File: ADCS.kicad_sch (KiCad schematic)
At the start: 16 parts

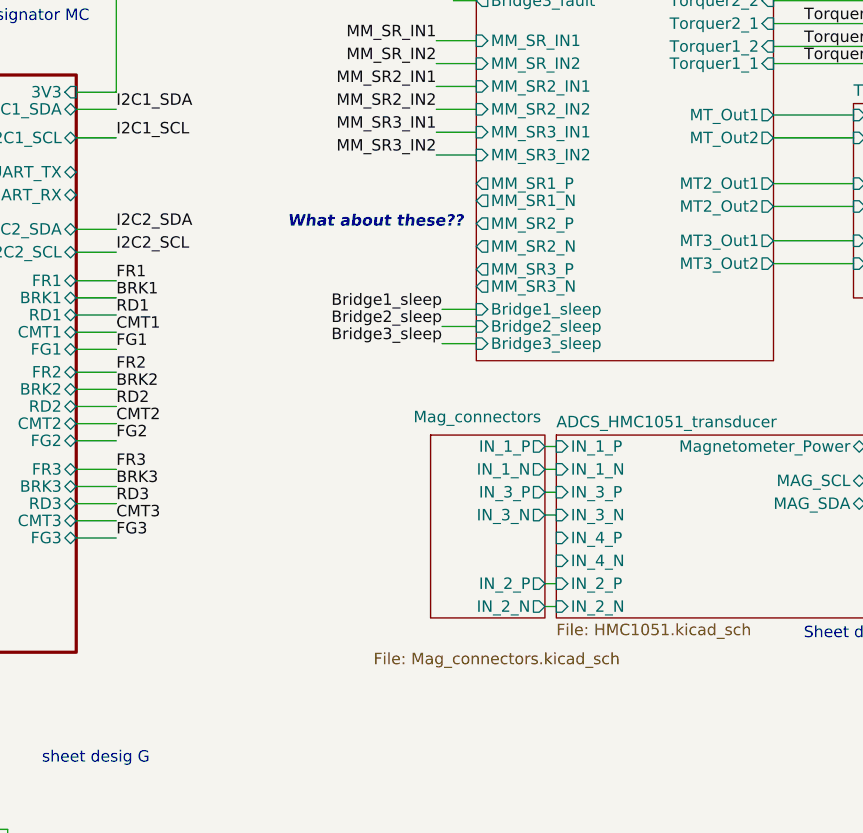
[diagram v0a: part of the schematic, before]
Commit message: Updated 8 pin connector for magentometer
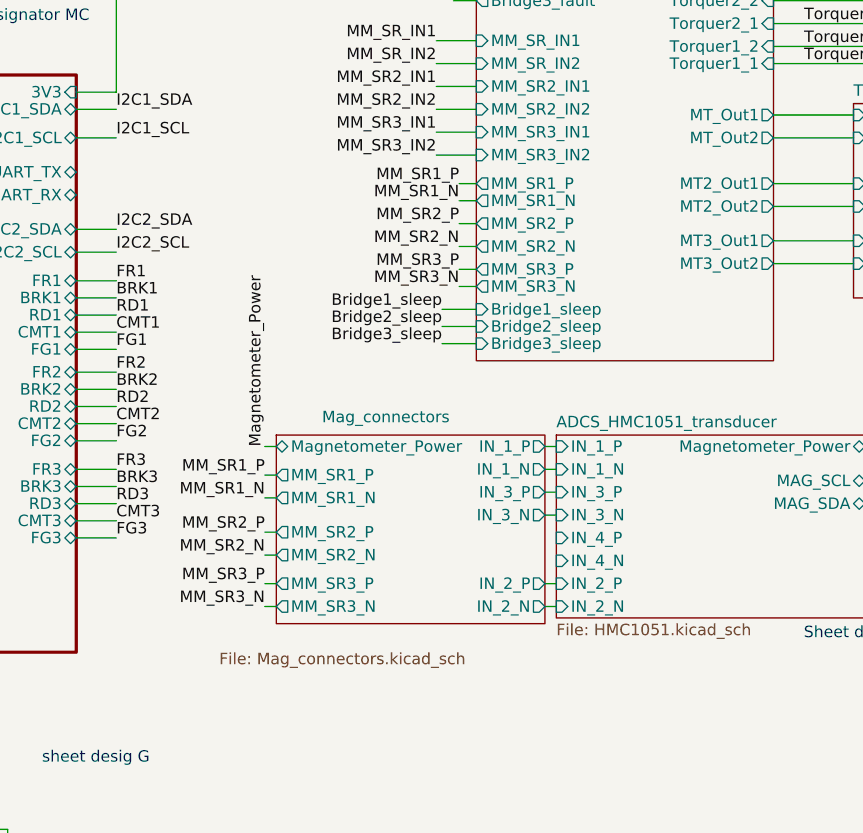
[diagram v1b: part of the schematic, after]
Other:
- sheet Mag_connectors ports: added MM_SR1_N, MM_SR1_P, MM_SR2_N, MM_SR2_P, MM_SR3_N, MM_SR3_P, Magnetometer_Power; removed none
- note removed: "What about these??"
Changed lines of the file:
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@@
     (stroke (width 0) (type default) (color 0 0 0 0))
   )
+  (wire (pts (xy 194.31 95.25) (xy 195.58 95.25))
+    (stroke (width 0) (type default) (color 0 0 0 0))
+  )
   (wire (pts (xy 215.265 38.1) (xy 217.805 38.1))
     (stroke (width 0) (type default) (color 0 0 0 0))
@@
     (stroke (width 0) (type default) (color 0 0 0 0))
   )
+  (wire (pts (xy 194.31 92.71) (xy 195.58 92.71))
+    (stroke (width 0) (type default) (color 0 0 0 0))
+  )
   (wire (pts (xy 157.48 33.655) (xy 161.29 33.655))
     (stroke (width 0) (type default) (color 0 0 0 0))
@@
     (stroke (width 0) (type default) (color 0 0 0 0))
   )
+  (wire (pts (xy 215.9 60.325) (xy 217.805 60.325))
+    (stroke (width 0) (type default) (color 0 0 0 0))
+  )
   (wire (pts (xy 161.925 135.89) (xy 161.925 139.7))
     (stroke (width 0) (type default) (color 0 0 0 0))
@@
     (stroke (width 0) (type default) (color 0 0 0 0))
   )
+  (wire (pts (xy 215.9 67.31) (xy 217.805 67.31))
+    (stroke (width 0) (type default) (color 0 0 0 0))
+  )
+  (wire (pts (xy 215.9 62.23) (xy 217.805 62.23))
+    (stroke (width 0) (type default) (color 0 0 0 0))
+  )
+  (wire (pts (xy 215.9 71.755) (xy 217.805 71.755))
+    (stroke (width 0) (type default) (color 0 0 0 0))
+  )
   (wire (pts (xy 19.685 80.01) (xy 23.495 80.01))
     (stroke (width 0) (type default) (color 0 0 0 0))
@@
     (stroke (width 0) (type default) (color 0 0 0 0))
   )
+  (wire (pts (xy 194.31 89.535) (xy 195.58 89.535))
+    (stroke (width 0) (type default) (color 0 0 0 0))
+  )
   (wire (pts (xy 127 105.41) (xy 130.81 105.41))
     (stroke (width 0) (type default) (color 0 0 0 0))
@@
     (stroke (width 0) (type default) (color 0 0 0 0))
   )
+  (wire (pts (xy 215.9 69.85) (xy 217.805 69.85))
+    (stroke (width 0) (type default) (color 0 0 0 0))
+  )
   (wire (pts (xy 22.225 100.33) (xy 23.495 100.33))
     (stroke (width 0) (type default) (color 0 0 0 0))
@@
     (stroke (width 0) (type default) (color 0 0 0 0))
   )
+  (wire (pts (xy 194.31 99.06) (xy 195.58 99.06))
+    (stroke (width 0) (type default) (color 0 0 0 0))
+  )
   (wire (pts (xy 48.895 102.87) (xy 48.895 92.71))
     (stroke (width 0) (type default) (color 0 0 0 0))
@@
     (stroke (width 0) (type default) (color 0 0 0 0))
   )
+  (wire (pts (xy 194.31 104.775) (xy 195.58 104.775))
+    (stroke (width 0) (type default) (color 0 0 0 0))
+  )
   (wire (pts (xy 121.92 130.81) (xy 126.365 130.81))
     (stroke (width 0) (type default) (color 0 0 0 0))
@@
     (stroke (width 0) (type default) (color 0 0 0 0))
   )
+  (wire (pts (xy 194.31 107.315) (xy 195.58 107.315))
+    (stroke (width 0) (type default) (color 0 0 0 0))
+  )
   (wire (pts (xy 215.265 36.195) (xy 217.805 36.195))
     (stroke (width 0) (type default) (color 0 0 0 0))
@@
     (stroke (width 0) (type default) (color 0 0 0 0))
   )
+  (wire (pts (xy 194.31 101.6) (xy 195.58 101.6))
+    (stroke (width 0) (type default) (color 0 0 0 0))
+  )
   (wire (pts (xy 173.355 71.12) (xy 177.8 71.12))
     (stroke (width 0) (type default) (color 0 0 0 0))
@@
     (stroke (width 0) (type default) (color 0 0 0 0))
   )
+  (wire (pts (xy 215.9 64.77) (xy 217.805 64.77))
+    (stroke (width 0) (type default) (color 0 0 0 0))
+  )
   (wire (pts (xy 60.325 72.39) (xy 62.865 72.39))
     (stroke (width 0) (type default) (color 0 0 0 0))
@@
     (effects (font (size 1.27 1.27)) (justify left bottom))
   )
-  (text "What about these??" (at 196.85 65.405 0)
-    (effects (font (size 1.27 1.27) (thickness 0.254) bold italic) (justify left bottom))
-  )
   (text "Sheet Designator R\n" (at 63.5 45.72 0)
     (effects (font (size 1.27 1.27)) (justify left bottom))
@@
     (effects (font (size 1.27 1.27)) (justify right bottom))
   )
+  (label "MM_SR1_N" (at 215.9 62.23 180)
+    (effects (font (size 1.27 1.27)) (justify right bottom))
+  )
   (label "I2C2_SDA" (at 102.235 21.59 180)
     (effects (font (size 1.27 1.27)) (justify right bottom))
@@
     (effects (font (size 1.27 1.27)) (justify right bottom))
   )
+  (label "MM_SR1_P" (at 215.9 60.325 180)
+    (effects (font (size 1.27 1.27)) (justify right bottom))
+  )
+  (label "MM_SR3_N" (at 194.31 107.315 180)
+    (effects (font (size 1.27 1.27)) (justify right bottom))
+  )
   (label "I2C1_SDA" (at 179.07 146.05 0)
     (effects (font (size 1.27 1.27)) (justify left bottom))
@@
     (effects (font (size 1.27 1.27)) (justify right bottom))
   )
+  (label "MM_SR2_P" (at 215.9 64.77 180)
+    (effects (font (size 1.27 1.27)) (justify right bottom))
+  )
   (label "MM_SR2_IN1" (at 128.27 84.455 180)
     (effects (font (size 1.27 1.27)) (justify right bottom))
@@
     (effects (font (size 1.27 1.27)) (justify right bottom))
   )
+  (label "MM_SR2_N" (at 215.9 67.31 180)
+    (effects (font (size 1.27 1.27)) (justify right bottom))
+  )
   (label "RD1" (at 177.8 74.93 0)
     (effects (font (size 1.27 1.27)) (justify left bottom))
@@
     (effects (font (size 1.27 1.27)) (justify left bottom))
   )
+  (label "MM_SR1_N" (at 194.31 95.25 180)
+    (effects (font (size 1.27 1.27)) (justify right bottom))
+  )
   (label "CMT1" (at 19.685 49.53 180)
     (effects (font (size 1.27 1.27)) (justify right bottom))
@@
     (effects (font (size 1.27 1.27)) (justify right bottom))
   )
+  (label "MM_SR3_N" (at 215.9 71.755 180)
+    (effects (font (size 1.27 1.27)) (justify right bottom))
+  )
   (label "V_bridge" (at 161.29 31.115 0)
     (effects (font (size 1.27 1.27)) (justify left bottom))
@@
     (effects (font (size 1.27 1.27)) (justify right bottom))
   )
+  (label "MM_SR1_P" (at 194.31 92.71 180)
+    (effects (font (size 1.27 1.27)) (justify right bottom))
+  )
   (label "MM_SR_IN1" (at 213.36 44.45 180)
     (effects (font (size 1.27 1.27)) (justify right bottom))
@@
     (effects (font (size 1.27 1.27)) (justify right bottom))
   )
+  (label "MM_SR3_P" (at 194.31 104.775 180)
+    (effects (font (size 1.27 1.27)) (justify right bottom))
+  )
   (label "MM_SR3_IN1" (at 213.36 54.61 180)
     (effects (font (size 1.27 1.27)) (justify right bottom))
   )
+  (label "MM_SR2_P" (at 194.31 99.06 180)
+    (effects (font (size 1.27 1.27)) (justify right bottom))
+  )
   (label "Bridge1_fault" (at 127 96.52 180)
     (effects (font (size 1.27 1.27)) (justify right bottom))
@@
     (effects (font (size 1.27 1.27)) (justify right bottom))
   )
+  (label "MM_SR2_N" (at 194.31 101.6 180)
+    (effects (font (size 1.27 1.27)) (justify right bottom))
+  )
   (label "MCU_POW" (at 22.225 71.12 180)
     (effects (font (size 1.27 1.27)) (justify right bottom))
@@
     (effects (font (size 1.143 1.143)) (justify right bottom))
   )
+  (label "MM_SR3_P" (at 215.9 69.85 180)
+    (effects (font (size 1.27 1.27)) (justify right bottom))
+  )
   (label "Bridge3_sleep" (at 213.995 78.105 180)
     (effects (font (size 1.27 1.27)) (justify right bottom))
@@
     (effects (font (size 1.27 1.27)) (justify left bottom))
   )
+  (label "Magnetometer_Power" (at 194.31 89.535 90)
+    (effects (font (size 1.27 1.27)) (justify left bottom))
+  )
   (label "I2C1_SCL" (at 177.8 142.875 0)
     (effects (font (size 1.27 1.27)) (justify left bottom))
@@
     )
   )
-  (sheet (at 212.725 88.265) (size 12.7 20.32)
+  (sheet (at 195.58 88.265) (size 29.845 20.955)
     (stroke (width 0.1524) (type solid) (color 0 0 0 0))
     (fill (color 173 230 255 1.0000))
-    (property "Sheet name" "Mag_connectors" (id 0) (at 210.82 86.995 0)
+    (property "Sheet name" "Mag_connectors" (id 0) (at 200.66 86.995 0)
       (effects (font (size 1.27 1.27)) (justify left bottom))
     )
-    (property "Sheet file" "Mag_connectors.kicad_sch" (id 1) (at 206.375 112.395 0)
+    (property "Sheet file" "Mag_connectors.kicad_sch" (id 1) (at 189.23 112.395 0)
       (effects (font (size 1.27 1.27)) (justify left top))
     )
@@
       (effects (font (size 1.27 1.27)) (justify right))
     )
+    (pin "Magnetometer_Power" bidirectional (at 195.58 89.535 180)
+      (effects (font (size 1.27 1.27)) (justify left))
+    )
+    (pin "MM_SR1_P" output (at 195.58 92.71 180)
+      (effects (font (size 1.27 1.27)) (justify left))
+    )
+    (pin "MM_SR3_P" output (at 195.58 104.775 180)
+      (effects (font (size 1.27 1.27)) (justify left))
+    )
+    (pin "MM_SR2_N" output (at 195.58 101.6 180)
+      (effects (font (size 1.27 1.27)) (justify left))
+    )
+    (pin "MM_SR1_N" output (at 195.58 95.25 180)
+      (effects (font (size 1.27 1.27)) (justify left))
+    )
+    (pin "MM_SR2_P" output (at 195.58 99.06 180)
+      (effects (font (size 1.27 1.27)) (justify left))
+    )
+    (pin "MM_SR3_N" output (at 195.58 107.315 180)
+      (effects (font (size 1.27 1.27)) (justify left))
+    )
   )
   (sheet (at 226.695 88.265) (size 34.29 20.32) (fields_autoplaced)
@@
       (reference "#PWR0264") (unit 1) (value "GND") (footprint "")
     )
+    (path "/90eea1cc-3897-47cb-b6ba-95228c17b7e0/9b0b7e65-9fe2-4923-805e-2058d79ef8cd"
+      (reference "#PWR?") (unit 1) (value "GND") (footprint "")
+    )
+    (path "/90eea1cc-3897-47cb-b6ba-95228c17b7e0/fee31364-d497-434e-aba3-d9001da3381e"
+      (reference "#PWR?") (unit 1) (value "GND") (footprint "")
+    )
     (path "/85fce53c-db5d-41a5-af86-f02ad1af70e7/c2b51706-9b59-4979-b562-badd0d98848a"
       (reference "CA3") (unit 1) (value "2.2u") (footprint "")
@@
       (reference "JSC6") (unit 1) (value "2367196-8") (footprint "")
     )
+    (path "/90eea1cc-3897-47cb-b6ba-95228c17b7e0/a754a1e4-2f8d-40cf-a07f-bdf1f085778f"
+      (reference "JSC?") (unit 1) (value "2367196-8") (footprint "")
+    )
     (path "/4d1fba12-6ef0-42d4-9064-f9f362dde9b9/8656cb07-b7b7-4825-942a-87872d0ebb27"

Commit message: Updated the changes
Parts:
- gave numbers to parts that had none: 2
- renumbered R7 to R10, R8 to R11, R9 to R12, R10 to R13, R11 to R14, R14 to R2, R2 to R3, R3 to R4, R4 to R5, R5 to R6, R12 to R7, R13 to R8, R6 to R9
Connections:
- no-connect marks 0 -> 4

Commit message: magnetometer connector corrected
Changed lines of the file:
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@@
     (effects (font (size 1.27 1.27)) (justify left bottom))
   )
-  (text "sheet desig G\n\n" (at 169.545 127 0)
+  (text "sheet desig G\n\n" (at 200.66 119.38 0)
     (effects (font (size 1.27 1.27)) (justify left bottom))
   )
@@
       (reference "#PWR0149") (unit 1) (value "GND") (footprint "")
     )
-    (path "/90eea1cc-3897-47cb-b6ba-95228c17b7e0/af365d8d-45a0-4279-b9aa-e85ef081cff1"
-      (reference "#PWR0150") (unit 1) (value "GND") (footprint "")
-    )
-    (path "/90eea1cc-3897-47cb-b6ba-95228c17b7e0/9b0b7e65-9fe2-4923-805e-2058d79ef8cd"
-      (reference "#PWR0151") (unit 1) (value "GND") (footprint "")
-    )
-    (path "/90eea1cc-3897-47cb-b6ba-95228c17b7e0/fee31364-d497-434e-aba3-d9001da3381e"
-      (reference "#PWR0152") (unit 1) (value "GND") (footprint "")
-    )
-    (path "/90eea1cc-3897-47cb-b6ba-95228c17b7e0/d212d134-095c-4203-b1ec-5eee87c1621f"
-      (reference "#PWR0153") (unit 1) (value "GND") (footprint "")
-    )
-    (path "/90eea1cc-3897-47cb-b6ba-95228c17b7e0/b3290ea7-02f6-47a6-9a50-5235251e13f0"
-      (reference "#PWR0154") (unit 1) (value "GND") (footprint "")
-    )
     (path "/7a353e73-f362-4813-b2c3-9e73ce7ee8de/2e2e80b8-f5cb-4c8f-ae78-85b5504fc930"
       (reference "#PWR0155") (unit 1) (value "GND") (footprint "")
@@
       (reference "#PWR0166") (unit 1) (value "GND") (footprint "")
     )
+    (path "/90eea1cc-3897-47cb-b6ba-95228c17b7e0/08c4494f-9f1c-4926-98e0-493f36ae8c45"
+      (reference "#PWR?") (unit 1) (value "GND") (footprint "")
+    )
+    (path "/90eea1cc-3897-47cb-b6ba-95228c17b7e0/1252f635-9880-4113-b5ba-9f84c80cbab9"
+      (reference "#PWR?") (unit 1) (value "GND") (footprint "")
+    )
+    (path "/90eea1cc-3897-47cb-b6ba-95228c17b7e0/35c6e339-688e-4d33-b782-0f842ecaf145"
+      (reference "#PWR?") (unit 1) (value "GND") (footprint "")
+    )
+    (path "/90eea1cc-3897-47cb-b6ba-95228c17b7e0/88ef94b4-1b3f-401a-83e5-5c6f167ecc62"
+      (reference "#PWR?") (unit 1) (value "GND") (footprint "")
+    )
+    (path "/90eea1cc-3897-47cb-b6ba-95228c17b7e0/af23a520-9df9-4aa5-a154-984e849ef1cd"
+      (reference "#PWR?") (unit 1) (value "GND") (footprint "")
+    )
+    (path "/90eea1cc-3897-47cb-b6ba-95228c17b7e0/d8b1e183-4a7e-4bfc-b021-61453d4dff31"
+      (reference "#PWR?") (unit 1) (value "GND") (footprint "")
+    )
+    (path "/90eea1cc-3897-47cb-b6ba-95228c17b7e0/fc788ebe-5dce-4622-8be8-21cfa0e0f58b"
+      (reference "#PWR?") (unit 1) (value "GND") (footprint "")
+    )
     (path "/85fce53c-db5d-41a5-af86-f02ad1af70e7/c2b51706-9b59-4979-b562-badd0d98848a"
       (reference "CA1") (unit 1) (value "2.2u") (footprint "")
@@
       (reference "J1") (unit 1) (value "Conn_ARM_JTAG_SWD_10") (footprint "")
     )
+    (path "/90eea1cc-3897-47cb-b6ba-95228c17b7e0/7ae0ea39-15a3-49ee-88f8-3c5d1257d0ba"
+      (reference "JG1") (unit 1) (value "2367196-8") (footprint "")
+    )
+    (path "/90eea1cc-3897-47cb-b6ba-95228c17b7e0/1bc11220-d6f7-4e24-8cab-a4916ce3b99d"
+      (reference "JG2") (unit 1) (value "2367196-8") (footprint "")
+    )
+    (path "/90eea1cc-3897-47cb-b6ba-95228c17b7e0/2603eb9b-6e9b-417a-8f50-c76a9c1fc121"
+      (reference "JG3") (unit 1) (value "2367196-8") (footprint "")
+    )
     (path "/8fa611b7-cf75-4378-bd5d-72096b0e3078/97355b07-3b0f-4286-b37c-a4c08e6a759a"
       (reference "JIB1") (unit 1) (value "2367196-8") (footprint "")
     )
-    (path "/90eea1cc-3897-47cb-b6ba-95228c17b7e0/4258d828-95d7-4ac0-9c18-738f3bf4ca4e"
-      (reference "JM1") (unit 1) (value "502352-0210") (footprint "")
-    )
-    (path "/90eea1cc-3897-47cb-b6ba-95228c17b7e0/85986521-380c-46b6-84df-2f18d65ade2d"
-      (reference "JM2") (unit 1) (value "502352-0210") (footprint "")
-    )
-    (path "/90eea1cc-3897-47cb-b6ba-95228c17b7e0/751c002d-c9ed-4f6f-bf56-77d36fe6f8f9"
-      (reference "JM3") (unit 1) (value "502352-0210") (footprint "")
-    )
-    (path "/90eea1cc-3897-47cb-b6ba-95228c17b7e0/a754a1e4-2f8d-40cf-a07f-bdf1f085778f"
-      (reference "JSC1") (unit 1) (value "2367196-8") (footprint "")
-    )
     (path "/7a353e73-f362-4813-b2c3-9e73ce7ee8de/c0b6aae2-d2fb-4c24-8018-c87793aa0bc5"
